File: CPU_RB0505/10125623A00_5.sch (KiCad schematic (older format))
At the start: 48 parts, among them IC21 LT1236ACS8-5, IC23 LT1236ACS8-10, IC24 STM809LWX, IC25 STM809LWX, IC26 LF33CDT, IC29 TPS5430, IC36 STM809TWX, T10 FZT953, T11 FZT953, T12 FZT953

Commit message: CPU schematic updated to Kicad resistor and cap symbols
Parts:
- C105, C107, C46, C47, C74, C79, C80, C82, C83, C90, C91, C97: symbol cpu-board:C0805 -> Flipped_Devices:C_Small
- C108, C117, C92: symbol cpu-board:TANTALB -> Flipped_Devices:CP_Small
- C21, C88, ZC21: symbol cpu-board:MV100_F50V -> Flipped_Devices:CP_Small
- C81, C85: symbol cpu-board:TANTALD -> Flipped_Devices:CP_Small
- R35, R36, R40, R44, R66, R67, R71, R73: symbol cpu-board:R0805 -> Flipped_Devices:R
- R41: symbol cpu-board:R1206 -> Flipped_Devices:R
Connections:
- wire segments 180 -> 181

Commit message: CPU board diode and transistor symbols changed to Kicad symbols
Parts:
- C106, ZC106: symbol cpu-board:CHCMS_D8 -> Flipped_Devices:CP_Small
- D11: symbol cpu-board:BAT54 -> Flipped_Devices:D_Schottky_A1K3
- D4: symbol cpu-board:ICTE5 -> Flipped_Devices:D_Schottky_Small
- D7: symbol cpu-board:PRLL5819 -> Flipped_Devices:D_Schottky
- L30: symbol cpu-board:7427504 -> Flipped_Devices:L
- T10, T11, T12: symbol cpu-board:BCP51 -> Device:Q_PNP_BCEC
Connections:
- wire segments 181 -> 180

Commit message: ran renameSchSyms.py
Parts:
- C105, C46, C79, C82: symbol Flipped_Devices:C_Small -> Capacitor:C0805_100nF_50V_10%
- C106: symbol Flipped_Devices:CP_Small -> Capacitor:C_220uF_20%
- C107, C74, C80, C83, C90, C91: symbol Flipped_Devices:C_Small -> Capacitor:C0402_100nF_16V_10%
- C108, C81, C85: symbol Flipped_Devices:CP_Small -> Capacitor:C_10uF_25V_10%
- C117: symbol Flipped_Devices:CP_Small -> Capacitor:C_10uF_50V_10%
- C21: symbol Flipped_Devices:CP_Small -> Capacitor:C_100uF_35V_20%
- C47: symbol Flipped_Devices:C_Small -> Capacitor:C0402_220pF_50V_5%
- C88: symbol Flipped_Devices:CP_Small -> Capacitor:C_1kF_35V_20%
- C92: symbol Flipped_Devices:CP_Small -> Capacitor:C_22uF_10V_10%
- C97: symbol Flipped_Devices:C_Small -> Capacitor:C0603_10nF_50V_10%
- D11: symbol Flipped_Devices:D_Schottky_A1K3 -> Diode:D_Schottky_A1K3_10022656
- D4: symbol Flipped_Devices:D_Schottky_Small -> Diode:D_Schottky_Small
- D7: symbol Flipped_Devices:D_Schottky -> Diode:D_Schottky
- FU2: symbol cpu-board:SLOBLO -> Fuse:SLOBLO
- IC21: symbol cpu-board:LT1236 -> IC:LT1236_10023039
- IC23: symbol cpu-board:LT1236 -> IC:LT1236_10023040
- IC24, IC25: symbol cpu-board:STM809 -> IC:STM809_10022974
- IC26: symbol cpu-board:LF33CDT -> IC:LF33CDT
- IC29: symbol cpu-board:TPS5430DDA -> IC:TPS5430DDA
- IC36: symbol cpu-board:STM809 -> IC:STM809_10023041
- L2: symbol cpu-board:WE-TPC-MH -> Inductor:WE-TPC-MH
- L30: symbol Flipped_Devices:L -> Inductor:L_10023186
- R35, R44: symbol Flipped_Devices:R -> Resistor:R0805_180R_5%
- R36: symbol Flipped_Devices:R -> Resistor:R0603_75k_1%
- R40: symbol Flipped_Devices:R -> Resistor:R0603_15k_1%
- R41: symbol Flipped_Devices:R -> Resistor:R_4k7_5%
- R66, R67: symbol Flipped_Devices:R -> Resistor:R0805_470R_1%
- R71: symbol Flipped_Devices:R -> Resistor:R0603_10k_0.1%_10097272
- R73: symbol Flipped_Devices:R -> Resistor:R0603_3k24_0.1%_10097273
- T10, T11, T12: symbol Device:Q_PNP_BCEC -> Transistor:Q_PNP_BCEC
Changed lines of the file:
@@
 $EndComp
 $Comp
-L Flipped_Devices:D_Schottky_Small D4
+L Diode:D_Schottky_Small D4
 U 1 1 C08B3BB7
 P 11650 2350
@@
 $EndComp
 $Comp
-L Flipped_Devices:C_Small C79
+L Capacitor:C0805_100nF_50V_10% C79
 U 1 1 5EA262E6
 P 1600 2500
@@
 $EndComp
 $Comp
-L Flipped_Devices:C_Small C82
+L Capacitor:C0805_100nF_50V_10% C82
 U 1 1 3B4E26FC
 P 1600 4900
@@
 $EndComp
 $Comp
-L Flipped_Devices:C_Small C105
+L Capacitor:C0805_100nF_50V_10% C105
 U 1 1 DFA69215
 P 2000 9450
@@
 $EndComp
 $Comp
-L Flipped_Devices:C_Small C91
+L Capacitor:C0402_100nF_16V_10% C91
 U 1 1 3BD8044E
 P 2450 6750
@@
 $EndComp
 $Comp
-L Flipped_Devices:C_Small C90
+L Capacitor:C0402_100nF_16V_10% C90
 U 1 1 8D21F230
 P 3500 6750
@@
 $EndComp
 $Comp
-L Flipped_Devices:C_Small C107
+L Capacitor:C0402_100nF_16V_10% C107
 U 1 1 21969A4D
 P 6050 8400
@@
 $EndComp
 $Comp
-L Flipped_Devices:D_Schottky D7
+L Diode:D_Schottky D7
 U 1 1 11F28FEE
 P 1700 9000
@@
 $EndComp
 $Comp
-L Flipped_Devices:D_Schottky_A1K3 D11
+L Diode:D_Schottky_A1K3_10022656 D11
 U 1 1 84A4DC5F
 P 2600 8100
@@
 $EndComp
 $Comp
-L Flipped_Devices:R R44
+L Resistor:R0805_180R_5% R44
 U 1 1 84674E91
 P 2100 4650
@@
 $EndComp
 $Comp
-L Flipped_Devices:R R71
+L Resistor:R0603_10k_0.1%_10097272 R71
 U 1 1 58DA2A05
 P 4750 9150
@@
 $EndComp
 $Comp
-L Flipped_Devices:R R73
+L Resistor:R0603_3k24_0.1%_10097273 R73
 U 1 1 EBEFFEA5
 P 4750 10150
@@
 $EndComp
 $Comp
-L Flipped_Devices:R R66
+L Resistor:R0805_470R_1% R66
 U 1 1 DA816598
 P 8150 3900
@@
 $EndComp
 $Comp
-L Flipped_Devices:R R67
+L Resistor:R0805_470R_1% R67
 U 1 1 2547CA40
 P 8450 4600
@@
 $EndComp
 $Comp
-L Flipped_Devices:R R40
+L Resistor:R0603_15k_1% R40
 U 1 1 7FF0BFE4
 P 15150 2750
@@
 $EndComp
 $Comp
-L cpu-board:WE-TPC-MH L2
+L Inductor:WE-TPC-MH L2
 U 1 1 86B7B564
 P 3650 8100
@@
 $EndComp
 $Comp
-L Flipped_Devices:CP_Small C88
+L Capacitor:C_1kF_35V_20% C88
 U 1 1 2D29FFA4
 P 1700 9800
@@
 $EndComp
 $Comp
-L Flipped_Devices:CP_Small C92
+L Capacitor:C_22uF_10V_10% C92
 U 1 1 939B92B5
 P 3900 6750
@@
 $EndComp
 $Comp
-L Flipped_Devices:CP_Small C106
+L Capacitor:C_220uF_20% C106
 U 1 1 F8977F3B
 P 4950 8400
@@
 $EndComp
 $Comp
-L Flipped_Devices:CP_Small C108
+L Capacitor:C_10uF_25V_10% C108
 U 1 1 1DA7F1EB
 P 5500 8400
@@
 $EndComp
 $Comp
-L Flipped_Devices:CP_Small C21
+L Capacitor:C_100uF_35V_20% C21
 U 1 1 967DA045
 P 14150 2300
@@
 $EndComp
 $Comp
-L Device:Q_PNP_BCEC T11
+L Transistor:Q_PNP_BCEC T11
 U 1 1 64295267
 P 2400 1450
@@
 $EndComp
 $Comp
-L Device:Q_PNP_BCEC T12
+L Transistor:Q_PNP_BCEC T12
 U 1 1 28298AA4
 P 2400 3850
@@
 $EndComp
 $Comp
-L Device:Q_PNP_BCEC T10
+L Transistor:Q_PNP_BCEC T10
 U 1 1 97227110
 P 12400 2100
@@
 $EndComp
 $Comp
-L cpu-board:LF33CDT IC26
+L IC:LF33CDT IC26
 U 1 1 694A8893
 P 2950 6400
@@
 $EndComp
 $Comp
-L cpu-board:LT1236 IC23
+L IC:LT1236_10023040 IC23
 U 1 1 44FE90A9
 P 2950 4500
@@
 $EndComp
 $Comp
-L cpu-board:STM809 IC24
+L IC:STM809_10022974 IC24
 U 1 1 7AE97733
 P 8950 2300
@@
 $EndComp
 $Comp
-L cpu-board:STM809 IC36
+L IC:STM809_10023041 IC36
 U 1 1 28D53763
 P 8950 6950
@@
 $EndComp
 $Comp
-L Flipped_Devices:CP_Small C85
+L Capacitor:C_10uF_25V_10% C85
 U 1 1 2D7C5423
 P 3950 4900
@@
 $EndComp
 $Comp
-L Flipped_Devices:CP_Small C81
+L Capacitor:C_10uF_25V_10% C81
 U 1 1 5EA262E9
 P 3950 2500
@@
 $EndComp
 $Comp
-L Flipped_Devices:R R35
+L Resistor:R0805_180R_5% R35
 U 1 1 AB7C9AB4
 P 2150 2250
@@
 $EndComp
 $Comp
-L cpu-board:LT1236 IC21
+L IC:LT1236_10023039 IC21
 U 1 1 88F14A94
 P 2950 2100
@@
 	4000 6250 4000 6400
 $Comp
-L Flipped_Devices:CP_Small C117
+L Capacitor:C_10uF_50V_10% C117
 U 1 1 E481EE55
 P 2550 9450
@@
 Connection ~ 2850 8100
 $Comp
-L Flipped_Devices:C_Small C97
+L Capacitor:C0603_10nF_50V_10% C97
 U 1 1 F034F2C9
 P 3650 8450
@@
 	8750 1750 8750 1800
 $Comp
-L cpu-board:TPS5430DDA IC29
+L IC:TPS5430DDA IC29
 U 1 1 408852E0
 P 3600 9550
@@
 	1600 2600 1600 2800
 $Comp
-L Flipped_Devices:C_Small C80
+L Capacitor:C0402_100nF_16V_10% C80
 U 1 1 5EA262E8
 P 3500 2500
@@
 $EndComp
 $Comp
-L Flipped_Devices:C_Small C?
+L Capacitor:C0402_100nF_16V_10% C?
 U 1 1 5EA9F004
 P 3500 4900
@@
 	11650 3050 12400 3050
 $Comp
-L cpu-board:SLOBLO FU2
+L Fuse:SLOBLO FU2
 U 1 1 2106B4DB
 P 11950 2000
@@
 	12400 2300 12400 2500
 $Comp
-L Flipped_Devices:R R41
+L Resistor:R_4k7_5% R41
 U 1 1 5EAEEA7B
 P 12400 2650
@@
 $EndComp
 $Comp
-L Flipped_Devices:C_Small C47
+L Capacitor:C0402_220pF_50V_5% C47
 U 1 1 5EB01229
 P 13000 2300
@@
 $EndComp
 $Comp
-L Flipped_Devices:C_Small C46
+L Capacitor:C0805_100nF_50V_10% C46
 U 1 1 5EB01C7B
 P 13650 2300
@@
 $EndComp
 $Comp
-L Flipped_Devices:L L30
+L Inductor:L_10023186 L30
 U 1 1 5EAF932D
 P 13350 2000
@@
 Connection ~ 14150 2000
 $Comp
-L Flipped_Devices:R R?
+L Resistor:R0603_75k_1% R?
 U 1 1 5EB4CA51
 P 15150 2250
@@
 $EndComp
 $Comp
-L Flipped_Devices:C_Small C74
+L Capacitor:C0402_100nF_16V_10% C74
 U 1 1 5EB68398
 P 14900 2750
@@
 	8750 3900 8750 4050
 $Comp
-L cpu-board:STM809 IC25
+L IC:STM809_10022974 IC25
 U 1 1 6D5019AB
 P 8950 4550

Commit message: CPU board passed ERC and matches Update PCB report
Schematic needs cleanup!
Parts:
- C117: symbol Capacitor:C_10uF_50V_10% -> Capacitor:C_10uF_50V_10%_0
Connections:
- wire segments 180 -> 204
- no-connect marks 3 -> 1
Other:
- moved on the sheet: C105, C88, C97, D11, D7, IC29, L2

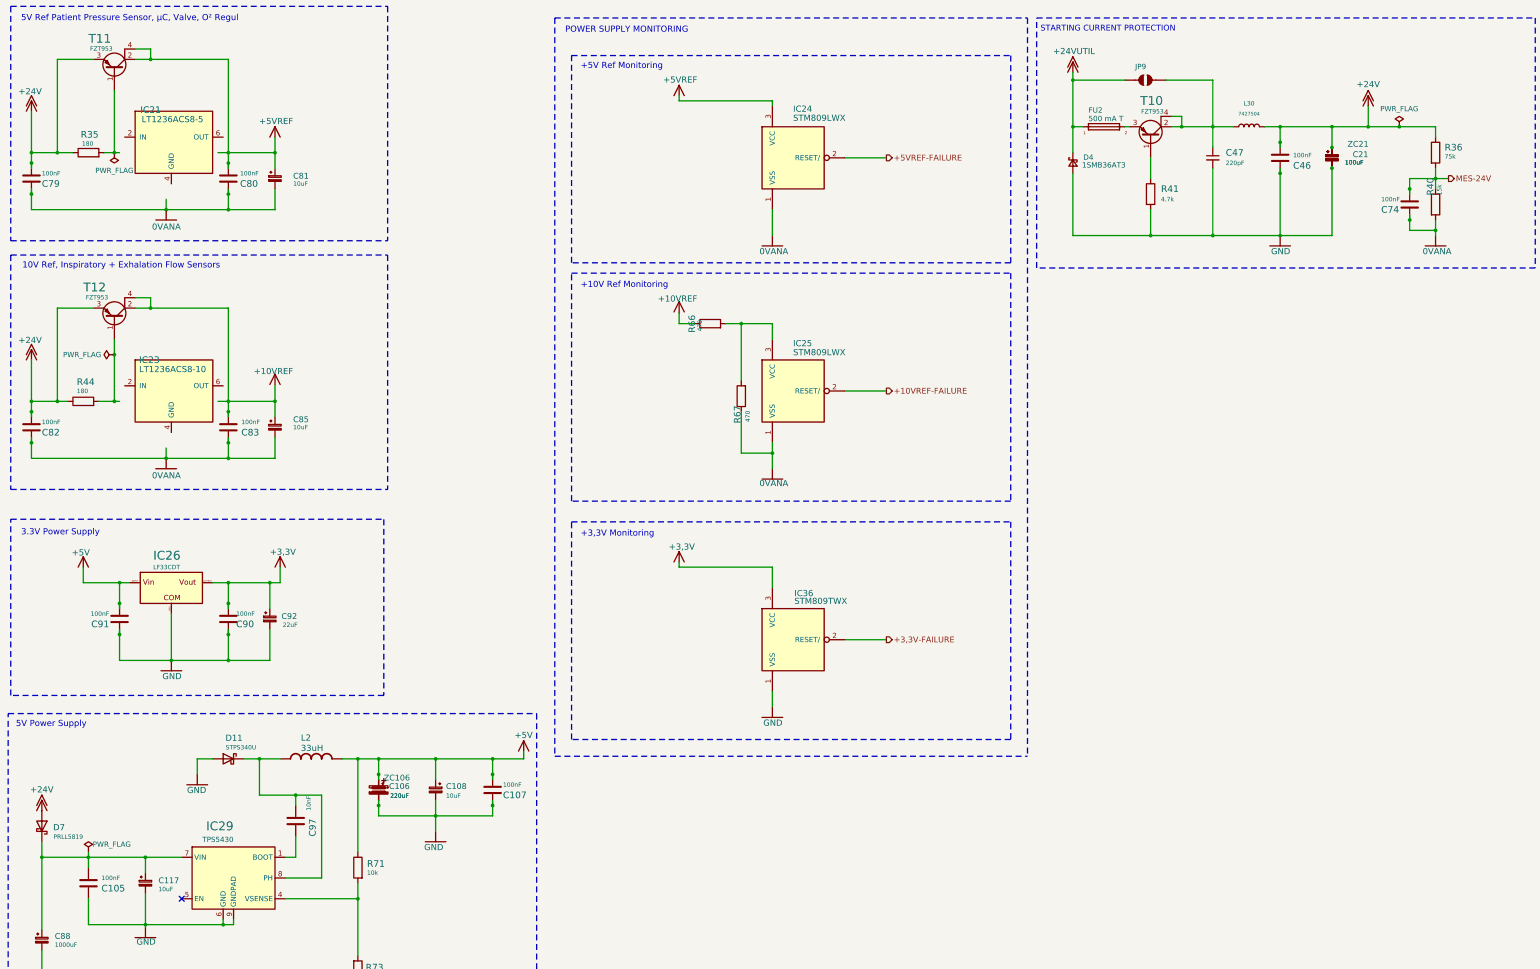
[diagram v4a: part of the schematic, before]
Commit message: Symbols and links update: sch page 5 and global lib
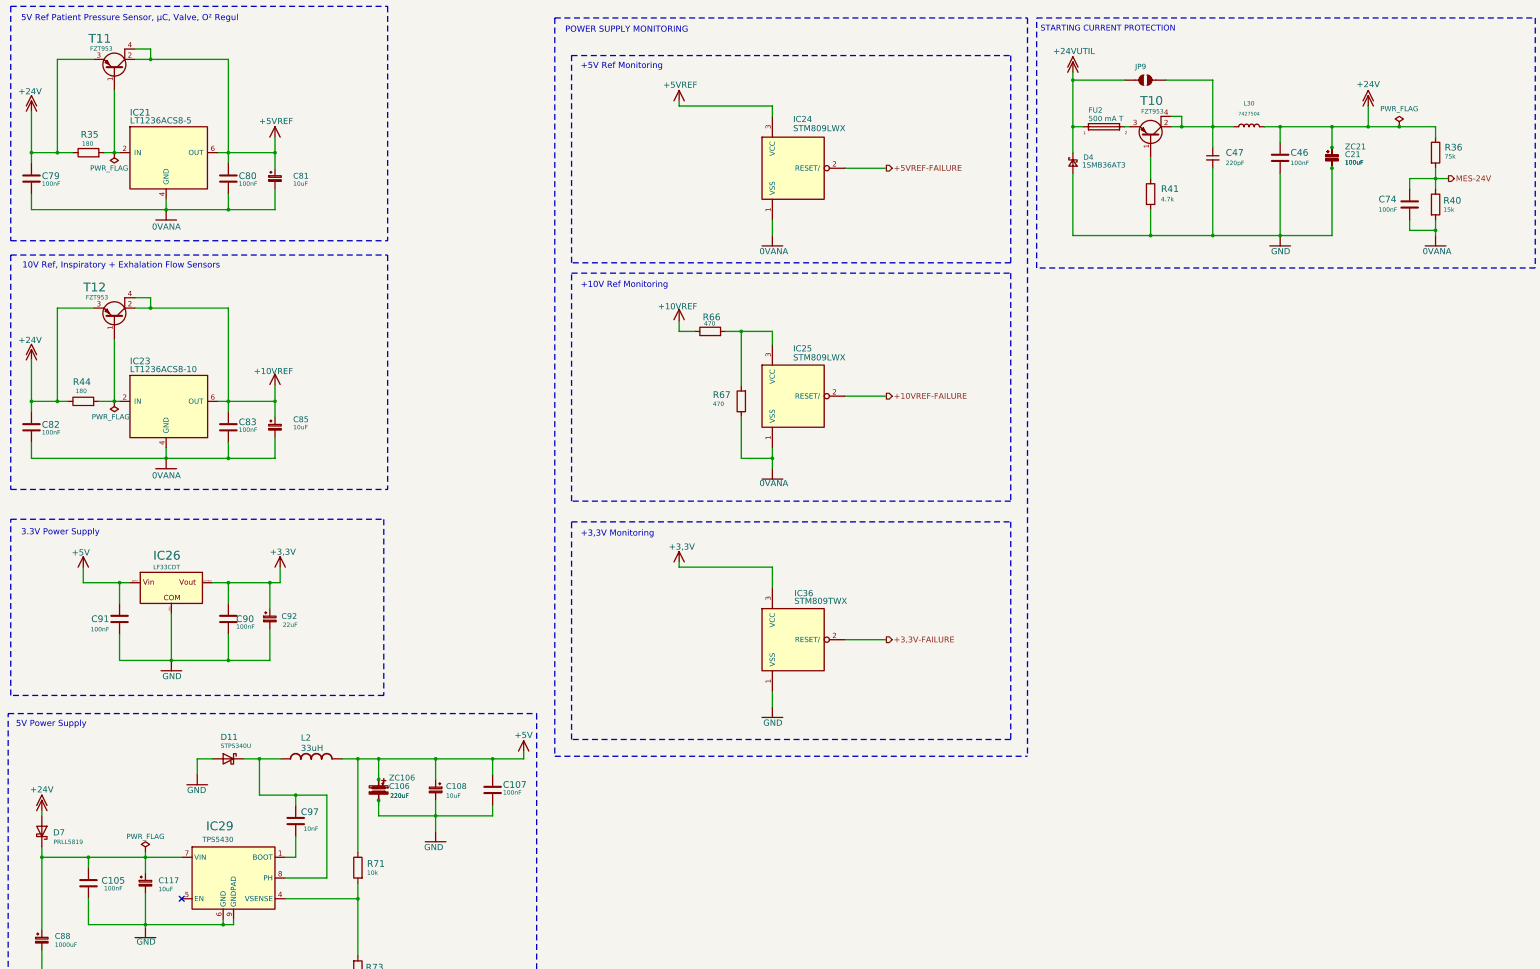
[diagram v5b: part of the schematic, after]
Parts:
- C105, C46, C79, C82: Manufacturer4 SAMSUNG_RMS1 -> (none); Manufacturer5 YAGEO_RMS1 -> (none); Manufacturer6 AVX_RMS1 -> (none); Manufacturer_Desc4 MULTILAYER CERAMIC CAPACITOR -> (none); Manufacturer_Desc5 CAP CER .1UF 50V 10% X7R 0805 -> (none); Manufacturer_Desc6 CAPACITOR CERAMIC, 100NF, +/-10%, 50V, X7R,0805, X7R DIELEC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 -> (none); Manufacturer_No4 CL21B104KBCNNNC -> (none); Manufacturer_No5 CC0805KRX7R9BB104 -> (none); Manufacturer_No6 08055C104KAT2A -> (none)
- C74, C80: Manufacturer4 MURATA MANUFACTURING CO., LTD. -> (none); Manufacturer_Desc4 MONOLITHIC CERAMIC CAPACITOR -> (none); Manufacturer_No4 GRM155R71C104KA88D -> (none)
- C97: Manufacturer4 YAGEO_RMS1 -> (none); Manufacturer_Desc4 CAPACITOR, CERAMIC, MULTILAYER, 50 V, X7R, 0.01 UF, SURFACE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 -> (none); Manufacturer_No4 CC0603KRX7R9BB103 -> (none)
- R35, R44: Manufacturer4 YAGEO_RMS1 -> (none); Manufacturer_Desc4 RESISTOR, METAL GLAZE/THICK FILM, 0.125 W, 5 %, 100 PPM, 18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 -> (none); Manufacturer_No4 RC0805JR-07180RL -> (none)
- R40: Manufacturer4 YAGEO_RMS1 -> (none); Manufacturer5 YAGEO_RMS1 -> (none); Manufacturer_Desc4 RESISTOR, METAL GLAZE/THICK FILM, 0.1 W, 1 %, 100 PPM, 1500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 -> (none); Manufacturer_Desc5 RESISTOR, METAL GLAZE/THICK FILM, 0.1 W, 1 %, 100 PPM, 1500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 -> (none); Manufacturer_No4 RC0603FR-0715KL -> (none); Manufacturer_No5 232270461503 -> (none)
- R41: Manufacturer4 YAGEO_RMS1 -> (none); Manufacturer_Desc4 RESISTOR, METAL GLAZE/THICK FILM, 0.1 W, 5 %, 100 PPM, 4700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 -> (none); Manufacturer_No4 232270260472 -> (none)
- R66, R67: Manufacturer4 YAGEO_RMS1 -> (none); Manufacturer5 ASJ -> (none); Manufacturer_Desc4 RESISTOR, METAL GLAZE/THICK FILM, 0.125 W, 1 %, 100 PPM, 47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 -> (none); Manufacturer_Desc5 THICK FILM CHIP RESISTOR -> (none); Manufacturer_No4 RC0805FR-07470RL -> (none); Manufacturer_No5 CR21-4700FL -> (none)
- R71: Manufacturer4 YAGEO_RMS1 -> (none); Manufacturer_No4 RT0603BRB0710KL -> (none)
- R73: Manufacturer4 YAGEO_RMS1 -> (none); Manufacturer_No4 RT0603BRD073K24L -> (none)
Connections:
- wire segments 204 -> 184
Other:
- moved on the sheet: D7, IC21, IC23, IC24, IC25, R66, R67

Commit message: Symbols and links update: sch page 4 and global lib
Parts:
- JP9: symbol cpu-board:JUMP_0U -> Jumper:JUMP_0U
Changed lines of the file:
@@
 $EndComp
 $Comp
-L cpu-board:JUMP_0U JP9
+L Jumper:JUMP_0U JP9
 U 1 1 C8B46213
 P 12350 1550

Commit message: Fixed 220uF cap ambiguity (cpu: C106/ZC106; pwrmgt: C44)
Used larger size symbol for both. Added a placeholder for TH version Item Number and Mfg data.
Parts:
- ZC106: symbol Flipped_Devices:CP_Small -> Capacitor:C_220uF_20%_TH
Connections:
- net at C107.2, C108.+ (1), L2.1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: now also C106.+
- net at C107.1, C108.- (2), ZC106.- (2): now also C106.-
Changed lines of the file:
@@
 $EndComp
 Wire Wire Line
-	4950 8100 4950 8300
-Wire Wire Line
-	4950 8500 4950 8650
-Connection ~ 4950 8500
-Connection ~ 4950 8300
+	4950 8100 4950 8250
 $Comp
-L Flipped_Devices:CP_Small C?
+L Capacitor:C_220uF_20%_TH C?
 U 1 1 5EA53F33
 P 4950 8400
@@
 	-1   0    0    -1
 $EndComp
+Wire Wire Line
+	4950 8550 4950 8650
+Connection ~ 4950 8250
+Connection ~ 4950 8550
 $EndSCHEMATC

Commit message: Fixed SMD caps with TH replacements. Appended "_TH" to ambigious Item Number
PwrMgt: C44, CPU: C21/ZC21, C106/ZC106
Renamed C_1kF to C1000uF
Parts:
- C106: symbol Capacitor:C_220uF_20% -> Capacitor:C_220uF_20%_SMD
- C21: symbol Capacitor:C_100uF_35V_20% -> Capacitor:C_100uF_50V_20%_SMD; Description CAPACITOR ELECTROLYTIC, 100UF, 35V +/-20% -> CAPACITOR,100UF,+/-20%,50V SMD; Manufacturer MULTICOMP (920630) -> NICHICON_RMS1; Manufacturer_No MCRH35V107M8X11 -> UWT1H101MNL1GS
- C88: symbol Capacitor:C_1kF_35V_20% -> Capacitor:C_1000uF_35V_20%
- ZC106: Item Number 10022622 -> 10022622_TH
- ZC21: symbol Flipped_Devices:CP_Small -> Capacitor:C_100uF_35V_20%_TH; Item Number 10022963 -> 10022963_TH; Manufacturer2 (none) -> LELON; Manufacturer_No (none) -> MCRH35V107M8X11; Manufacturer_No2 (none) -> RXW101M1VSA-0811
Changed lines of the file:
@@
 $EndComp
 $Comp
-L Capacitor:C_1kF_35V_20% C88
+L Capacitor:C_1000uF_35V_20% C88
 U 1 1 2D29FFA4
 P 1700 9850
@@
 $EndComp
 $Comp
-L Capacitor:C_100uF_35V_20% C21
+L Capacitor:C_100uF_50V_20%_SMD C21
 U 1 1 967DA045
 P 14150 2300
@@
 F 2 "AllModules:C-SC8_1" H 14150 2300 50  0001 C CNN
 F 3 "" H 14150 2300 50  0001 C CNN
-F 4 "CAPACITOR ELECTROLYTIC, 100UF, 35V +/-20%" H 14150 2300 50  0001 C CNN "Description"
+F 4 "CAPACITOR,100UF,+/-20%,50V SMD" H 14150 2300 50  0001 C CNN "Description"
 F 5 "10022963" H 14150 2300 50  0001 C CNN "Item Number"
-F 6 "MULTICOMP                       (920630)" H 14150 2300 50  0001 C CNN "Manufacturer"
-F 7 "MCRH35V107M8X11" H 14150 2300 50  0001 C CNN "Manufacturer_No"
+F 6 "NICHICON_RMS1" H 14150 2300 50  0001 C CNN "Manufacturer"
+F 7 "UWT1H101MNL1GS" H 14150 2300 50  0001 C CNN "Manufacturer_No"
 F 8 "ELECTROLYTIC CAPACITOR" H 14150 2300 50  0001 C CNN "Manufacturer_Desc"
 F 9 "LELON" H 14150 2300 50  0001 C CNN "Manufacturer2"
@@
 Connection ~ 13000 3050
 Wire Wire Line
-	14150 2400 14150 3050
-Wire Wire Line
 	14150 3050 13650 3050
 Connection ~ 13650 3050
@@
 	13650 2000 14150 2000
 Wire Wire Line
-	14150 2000 14150 2200
+	14150 2000 14150 2150
 Connection ~ 13650 2000
 Connection ~ 14150 2000
@@
 	7850 3875 7850 3975
 $Comp
-L Flipped_Devices:CP_Small C?
+L Capacitor:C_100uF_35V_20%_TH C?
 U 1 1 5EA4EF1D
 P 14150 2300
@@
 F 3 "" H 14150 2300 50  0001 C CNN
 F 4 "CAPACITOR ELECTROLYTIC, 100UF, 35V +/-20%" H 14150 2300 50  0001 C CNN "Description"
-F 5 "10022963" H 14150 2300 50  0001 C CNN "Item Number"
+F 5 "10022963_TH" H 14150 2300 50  0001 C CNN "Item Number"
 F 6 "MULTICOMP                       (920630)" H 14150 2300 50  0001 C CNN "Manufacturer"
-F 7 "ELECTROLYTIC CAPACITOR" H 14150 2300 50  0001 C CNN "Manufacturer_Desc"
-F 8 "" H 14150 2300 50  0001 C CNN "Manufacturer2"
-F 9 "" H 14150 2300 50  0001 C CNN "Manufacturer_No2"
-F 10 "ALUMINIUM ELECTROLYTIC CAPACITOR" H 14150 2300 50  0001 C CNN "Manufacturer_Desc2"
+F 7 "MCRH35V107M8X11" H 14150 2300 50  0001 C CNN "Manufacturer_No"
+F 8 "ELECTROLYTIC CAPACITOR" H 14150 2300 50  0001 C CNN "Manufacturer_Desc"
+F 9 "LELON" H 14150 2300 50  0001 C CNN "Manufacturer2"
+F 10 "RXW101M1VSA-0811" H 14150 2300 50  0001 C CNN "Manufacturer_No2"
+F 11 "ALUMINIUM ELECTROLYTIC CAPACITOR" H 14150 2300 50  0001 C CNN "Manufacturer_Desc2"
 	1    14150 2300
 	1    0    0    -1
@@
 Wire Wire Line
 	14900 2500 14900 2600
-Connection ~ 14150 2200
-Connection ~ 14150 2400
 Wire Wire Line
 	3350 8100 3200 8100
@@
 $EndComp
 $Comp
-L Capacitor:C_220uF_20% C106
+L Capacitor:C_220uF_20%_SMD C106
 U 1 1 F8977F3B
 P 4950 8400
@@
 F 3 "" H 4950 8400 50  0001 C CNN
 F 4 "CAPACITOR ELECTROLYTIC, 220UF,16V+/-20%" H 4950 8400 50  0001 C CNN "Description"
-F 5 "10022622" H 4950 8400 50  0001 C CNN "Item Number"
+F 5 "10022622_TH" H 4950 8400 50  0001 C CNN "Item Number"
 F 6 "" H 4950 8400 50  0001 C CNN "Manufacturer_Desc"
 F 7 "" H 4950 8400 50  0001 C CNN "Manufacturer2"
@@
 Connection ~ 4950 8250
 Connection ~ 4950 8550
+Wire Wire Line
+	14150 2450 14150 3050
+Connection ~ 14150 2150
+Connection ~ 14150 2450
 $EndSCHEMATC
